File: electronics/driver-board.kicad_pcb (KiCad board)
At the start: 4 copper layers, 40 x 40 mm, 55 parts, among them J1 Conn_01x01_Socket, J10 USB_C_Receptacle_USB2.0, J3 Conn_01x06, J4 Qwiic_RA, J5 Conn_02x03_Counter_Clockwise, J9 Conn_01x01_Socket, SW1 SW_Push, SW2 SW_Push, SW3 SW_Push, SW4 SW_Push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

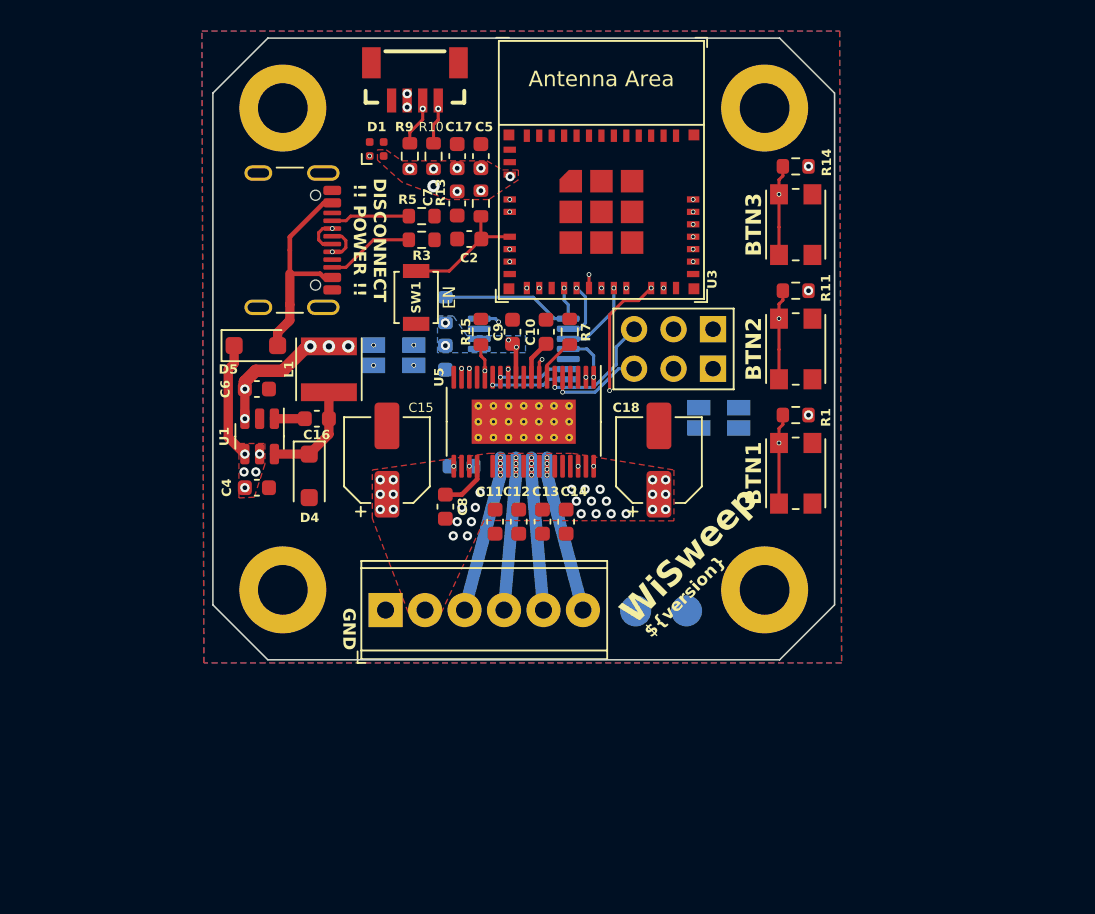
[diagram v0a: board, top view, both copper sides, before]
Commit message: added ldo for USB
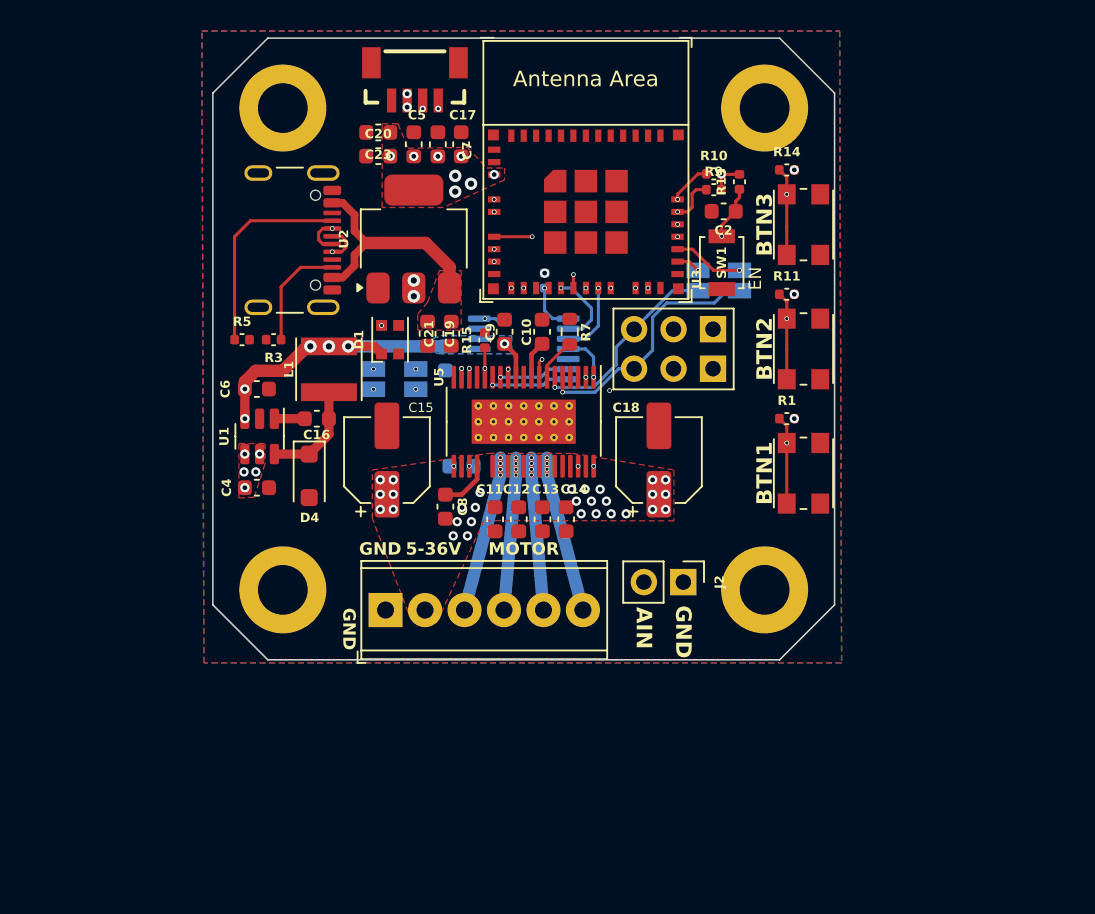
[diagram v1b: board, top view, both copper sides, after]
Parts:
- removed D5: DS210W, Diode_SMD:D_SOD-123F
- removed J1, J9: Conn_01x01_Socket, TestPoint:TestPoint_Pad_D2.0mm
- added C19: 100nF, Capacitor_SMD:C_0603_1608Metric, F.Cu at (43.8, 49.0)
- added C20: 10µF, Capacitor_SMD:C_0603_1608Metric, F.Cu at (40.6, 37.6)
- added C21: 10µF, Capacitor_SMD:C_0603_1608Metric, F.Cu at (45.3, 49.0)
- added C23: 100nF, Capacitor_SMD:C_0603_1608Metric, F.Cu at (40.6, 36.1)
- added J2: Conn_01x02, Connector_PinHeader_2.54mm:PinHeader_1x02_P2.54mm_Vertical, F.Cu at (60.3, 65.0)
- added U2: AMS1117-3.3, Package_TO_SOT_SMD:SOT-223-3_TabPin2, F.Cu at (42.9, 42.9)
- D1: footprint LED_SMD:LED_SK6812_EC15_1.5x1.5mm -> LED_SMD:LED_WS2812B-2020_PLCC4_2.0x2.0mm
- R1, R10, R11, R13, R14, R15, R2, R3, R5, R9: footprint Resistor_SMD:R_0603_1608Metric -> Capacitor_SMD:C_0402_1005Metric
- moved SW1 19.8 mm to (62.7, 44.5)
- moved R9 19.7 mm to (62.2, 39.8), turned to 0 degrees
- moved R10 18.1 mm to (62.2, 38.7), turned to 0 degrees
- moved R13 16.7 mm to (63.9, 39.2)
- moved C2 16.5 mm to (62.9, 41.1)
- moved R5 14.0 mm to (31.9, 49.4)
- moved D1 12.3 mm to (41.4, 49.4)
- moved R3 11.5 mm to (33.9, 49.4), turned to 180 degrees
- moved JP3 8.84 mm to (63.9, 45.6)
- moved JP4 8.84 mm to (61.2, 45.6)
- moved R2 6.66 mm to (51.3, 45.6), turned to 90 degrees
- moved C5 4.38 mm to (42.9, 36.8)
- moved C7 4.01 mm to (44.5, 36.8), turned to -90 degrees
- moved JP1 3.12 mm to (43.1, 51.9)
- moved JP2 3.01 mm to (40.3, 51.9)
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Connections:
- net /USB_VBUS renamed +5V
- net VBUS renamed VM
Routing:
- net /ESP_GPIO3: track 0.00 -> 23.5 mm
- net /TMC_AIN: track 1.22 -> 22.4 mm
- net +3V3: track 12.1 -> 27.9 mm, vias 22 -> 23
- net /ESP_GPIO1: track 0.00 -> 15.4 mm
- net /ESP_EN: track 8.41 -> 18.6 mm, vias 0 -> 2
- net /TMC_REFL: track 6.24 -> 16.3 mm
- net /ESP_GPIO2: track 11.0 -> 20.2 mm
- net /USB_CC1: track 5.06 -> 13.3 mm
- net VM: track 7.45 -> 0.00 mm
- net /ESP_GPIO6: track 10.6 -> 3.19 mm
- net /TMC_REFR: track 8.02 -> 13.2 mm
- net /ESP_GPIO21: track 0.00 -> 4.55 mm
- net /AS_ENCA: track 13.2 -> 10.1 mm
- net /AS_ENCB: track 10.5 -> 13.1 mm
- net /ESP_GPIO7: track 15.7 -> 17.3 mm
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- added copper zone on F.Cu, net +5V
- added copper zone on In1.Cu, net GND
- added copper zone on In2.Cu, net GND
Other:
- board text added: "MOTOR"
- board text removed: "${version}"
- board text removed: "DISCONNECT !! POWER !!"

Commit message: added few ground vias
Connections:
- J4 pad 3: /ESP_GPIO17 -> GND
- J4 pad 4: /ESP_GPIO16 -> GND
- R10 pad 1: /ESP_GPIO16 -> GND
- R9 pad 1: /ESP_GPIO17 -> GND
- U3 pad 30: /ESP_GPIO17 -> GND
- U3 pad 31: /ESP_GPIO16 -> GND
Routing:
- net GND: track 0.07 -> 45.7 mm, vias 0 -> 83
- net /ESP_GPIO17: track 23.7 -> 0.00 mm, vias 2 -> 0
- net /ESP_GPIO16: track 21.9 -> 0.00 mm, vias 2 -> 0
- net /AS_ENCN: track 5.65 -> 4.31 mm
- net VM: vias 34 -> 33

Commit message: reworked layout a bit
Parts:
- removed J2: Conn_01x02, Connector_PinHeader_2.54mm:PinHeader_1x02_P2.54mm_Vertical
- added C1: 100nF, Capacitor_SMD:C_0402_1005Metric, F.Cu at (41.4, 51.8)
- added C24: 100nF, Capacitor_SMD:C_0603_1608Metric, F.Cu at (76.7, 59.2)
- added D2: LESD5D5, Diode_SMD:D_SOD-523, B.Cu at (37.8, 42.2)
- added D6: LESD5D5, Diode_SMD:D_SOD-523, B.Cu at (37.8, 43.8)
- added R6: 10k, Resistor_SMD:R_0402_1005Metric, F.Cu at (76.2, 61.4)
- C22: moved to F.Cu
- R1, R10, R11, R13, R14, R2, R3, R5, R9: footprint Capacitor_SMD:C_0402_1005Metric -> Resistor_SMD:R_0402_1005Metric
- R15: footprint Capacitor_SMD:C_0402_1005Metric -> Resistor_SMD:R_0402_1005Metric; moved to B.Cu
- R7: footprint Resistor_SMD:R_0603_1608Metric -> Resistor_SMD:R_0402_1005Metric
- moved R15 3.56 mm to (48.7, 46.1), turned to 180 degrees
- moved C8 3.02 mm to (44.2, 57.2)
- moved C22 2.21 mm to (44.9, 59.5)
- moved R3 1.39 mm to (32.5, 49.6), turned to -90 degrees
- moved C9 1.12 mm to (48.4, 47.8), turned to 0 degrees
- moved R2 1.05 mm to (52.4, 45.6)
- moved R7 0.93 mm to (52.7, 48.0)
- moved D4 0.86 mm to (35.5, 58.7)
- moved L1 0.86 mm to (36.8, 51.8)
- moved C6 0.86 mm to (32.1, 53.1)
- moved U1 0.86 mm to (32.3, 56.1)
- moved C16 0.86 mm to (36.0, 55.0)
- moved JP2 0.81 mm to (39.5, 51.9)
- moved C15 0.70 mm to (40.5, 57.1)
- moved C18 0.70 mm to (59.4, 57.1)
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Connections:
- J4 pad 3: GND -> /ESP_GPIO17
- J4 pad 4: GND -> /ESP_GPIO16
- R10 pad 1: GND -> /ESP_GPIO16
- R2 pad 1: /ESP_GPIO6 -> /ESP_GPIO7
- R9 pad 1: GND -> /ESP_GPIO17
- U3 pad 30: GND -> /ESP_GPIO17
- U3 pad 31: GND -> /ESP_GPIO16
- U5 pad 1: /ESP_GPIO15 -> /ESP_GPIO14
- U5 pad 2: /ESP_GPIO14 -> /ESP_GPIO6
- U5 pad 36: /ESP_GPIO8 -> /ESP_GPIO15
- U5 pad 38: /ESP_GPIO7 -> /ESP_GPIO8
- U7 pad 1: /ESP_GPIO6 -> /ESP_GPIO7
- U7 pad 2: /ESP_GPIO7 -> /ESP_GPIO8
- U7 pad 3: /ESP_GPIO14 -> /ESP_GPIO6
- U7 pad 4: /ESP_GPIO15 -> /ESP_GPIO14
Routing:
- net GND: track 45.7 -> 0.00 mm, vias 83 -> 106
- net /ESP_GPIO17: track 0.00 -> 24.4 mm, vias 0 -> 2
- net /ESP_GPIO16: track 0.00 -> 22.9 mm, vias 0 -> 2
- net /ESP_GPIO7: track 17.3 -> 2.16 mm, vias 2 -> 1
- net /ESP_GPIO6: track 3.19 -> 11.3 mm, vias 1 -> 2
- net /ESP_GPIO8: track 13.0 -> 18.1 mm, vias 3 -> 2
- net /AS_ENCB: track 13.1 -> 18.1 mm
- net /ESP_GPIO1: track 15.4 -> 10.7 mm
- net /ESP_GPIO15: track 9.35 -> 13.2 mm
- net Net-(U5-CPI): track 0.00 -> 2.53 mm, vias 1 -> 0
- net /ESP_GPIO0: track 8.78 -> 6.26 mm, vias 2 -> 1
- net /BTN1: track 22.6 -> 20.3 mm
- net /AS_ENCA: track 10.1 -> 12.4 mm
- net Net-(U5-CPO): track 0.00 -> 2.26 mm, vias 1 -> 0
- net +3V3: track 27.9 -> 30.2 mm, vias 23 -> 27
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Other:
- board text added: "VM"
- board text removed: "MOTOR"

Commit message: wip usb jtag and power connectors
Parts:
- removed J3: Conn_01x06, TerminalBlock_Phoenix:TerminalBlock_Phoenix_MPT-0,5-6-2.54_1x06_P2.54mm_Horizontal
- removed R11, R14: 10k, Resistor_SMD:R_0402_1005Metric
- removed SW3, SW4: SW_Push, Slimc_Button_Switch_SMD:SW_Push_1P1T_TS-1145-X-B
- added J1: Conn_01x02, Connector_PinHeader_2.00mm:PinHeader_1x02_P2.00mm_Vertical_SMD_Pin1Left, B.Cu at (65.8, 48.6)
- added J2: Conn_01x03, Connector_JST:JST_SH_SM03B-SRSS-TB_1x03-1MP_P1.00mm_Horizontal, B.Cu at (54.0, 67.6)
- added J6: Conn_01x04, Connector_JST:JST_PH_S4B-PH-K_1x04_P2.00mm_Horizontal, F.Cu at (53.0, 63.5)
- added J7: Conn_01x03, Connector_JST:JST_SH_SM03B-SRSS-TB_1x03-1MP_P1.00mm_Horizontal, B.Cu at (46.0, 67.6)
- added R12: 10k, Resistor_SMD:R_0402_1005Metric, F.Cu at (58.8, 46.4)
- added R8: 10k, Resistor_SMD:R_0402_1005Metric, F.Cu at (58.8, 45.3)
- C24, R6: moved to B.Cu
- D2, D6: moved to F.Cu
- J10: footprint Connector_USB:USB_C_Receptacle_GCT_USB4105-xx-A_16P_TopMnt_Horizontal -> Slimc_Connector_USB:USB_C_GT-USB-7036A
- J4: footprint SparkFun-Connector:JST04_1MM_Vertical -> SparkFun-Connector:JST_SMD_1.0mm-4_RA
- J5: value Conn_02x03_Counter_Clockwise -> Conn_01x02; footprint Connector_PinHeader_2.54mm:PinHeader_2x03_P2.54mm_Vertical -> Connector_JST:JST_PH_S2B-PH-K_1x02_P2.00mm_Horizontal
- SW2: footprint Slimc_Button_Switch_SMD:SW_Push_1P1T_TS-1145-X-B -> Button_Switch_SMD:SW_SPST_B3U-1000P
- moved C4 49.5 mm to (82.2, 57.0), turned to -90 degrees
- moved U1 46.6 mm to (78.9, 57.5), turned to 0 degrees
- moved D4 46.1 mm to (81.4, 54.3), turned to 0 degrees
- moved C6 43.9 mm to (75.8, 57.6), turned to -90 degrees
- moved C16 41.8 mm to (77.7, 53.8), turned to -90 degrees
- moved L1 37.8 mm to (74.5, 53.0), turned to 180 degrees
- moved SW2 27.2 mm to (56.3, 33.5)
- moved C17 25.0 mm to (21.1, 39.7)
- moved C7 25.0 mm to (19.7, 39.7)
- moved J4 23.1 mm to (65.2, 38.8)
- moved C5 22.7 mm to (21.1, 42.7), turned to 90 degrees
- moved C1 22.5 mm to (63.9, 52.0)
- moved R1 21.6 mm to (61.3, 33.7), turned to -90 degrees
- moved J5 21.5 mm to (46.9, 63.5), turned to 0 degrees
- moved J10 20.7 mm to (40.9, 62.5), turned to 0 degrees
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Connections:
- net /BTN1 renamed /ESP_BOOT
- J5 pad 2: GND -> VM
- U3 pad 28: /BTN2 -> /ESP_GPIO22
- U3 pad 29: /BTN3 -> /ESP_GPIO23
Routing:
- net /ESP_GPIO17: track 24.4 -> 0.00 mm, vias 2 -> 0
- net +3V3: track 30.2 -> 6.68 mm, vias 27 -> 10
- net /ESP_GPIO3: track 23.0 -> 0.00 mm, vias 2 -> 0
- net /ESP_GPIO16: track 22.9 -> 0.00 mm, vias 2 -> 0
- net /TMC_AIN: track 21.4 -> 0.00 mm, vias 2 -> 0
- net /ESP_GPIO12: track 20.5 -> 0.00 mm, vias 2 -> 0
- net /ESP_GPIO2: track 20.5 -> 0.00 mm, vias 2 -> 0
- net /ESP_BOOT: track 20.3 -> 0.00 mm, vias 2 -> 0
- net /ESP_GPIO13: track 18.9 -> 0.00 mm, vias 2 -> 0
- net /ESP_EN: track 18.5 -> 0.00 mm, vias 2 -> 1
- net /ESP_GPIO8: track 18.1 -> 0.00 mm, vias 2 -> 0
- net /AS_ENCB: track 18.1 -> 0.00 mm, vias 2 -> 0
- net /TMC_REFL: track 17.7 -> 0.00 mm
- net /BTN2: track 15.5 -> 0.00 mm, vias 2 -> 0
- net +5V: track 14.9 -> 0.00 mm
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- removed copper zone on F.Cu, net +3V3
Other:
- board size 40 x 40 mm -> 38.5 x 39.6 mm
- board text added: "IO22"
- board text added: "IO23"
- board text added: "IO9"
- board text added: "NTC"
- board text added: "S"
- board text removed: "AIN"
- board text removed: "BTN1"
- board text removed: "BTN2"
- board text removed: "BTN3"

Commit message: testing new layout
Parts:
- removed C19, C23: 100nF, Capacitor_SMD:C_0603_1608Metric
- removed C20, C21: 10µF, Capacitor_SMD:C_0603_1608Metric
- removed U2: AMS1117-3.3, Package_TO_SOT_SMD:SOT-223-3_TabPin2
- J2, J7: moved to F.Cu
- moved C4 48.3 mm to (34.0, 60.5), turned to 180 degrees
- moved U1 45.3 mm to (33.6, 57.2), turned to -90 degrees
- moved D4 45.0 mm to (36.7, 59.7), turned to -90 degrees
- moved C6 42.6 mm to (33.4, 54.1), turned to 180 degrees
- moved C16 40.6 mm to (37.2, 56.0), turned to 180 degrees
- moved L1 36.5 mm to (38.0, 52.9), turned to 90 degrees
- moved R13 35.8 mm to (39.0, 34.4), turned to 180 degrees
- moved R10 33.6 mm to (41.9, 47.2), turned to -90 degrees
- moved R9 32.6 mm to (41.9, 45.3), turned to 90 degrees
- moved C2 32.4 mm to (41.4, 34.7), turned to 0 degrees
- moved J7 30.8 mm to (61.5, 41.0), turned to 90 degrees
- moved J4 25.1 mm to (40.4, 42.7), turned to -90 degrees
- moved C7 21.9 mm to (41.4, 37.6), turned to 0 degrees
- moved J2 21.5 mm to (61.5, 47.5), turned to 90 degrees
- moved C5 20.6 mm to (41.4, 39.1), turned to 0 degrees
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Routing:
- net GND: track 0.00 -> 17.3 mm
- net /TMC_OUT1B: track 20.7 -> 12.0 mm
- net /TMC_OUT1A: track 20.7 -> 12.0 mm
- net /TMC_OUT2B: track 19.9 -> 11.6 mm
- net VM: track 0.00 -> 8.26 mm
- net /ESP_GPIO12: track 0.00 -> 1.15 mm
- net /TMC_OUT2A: track 19.9 -> 18.7 mm
- net +3V3: vias 10 -> 7
- net /ESP_GPIO5: vias 1 -> 0
- net /ESP_GPIO21: vias 1 -> 0
- net /ESP_GPIO1: vias 1 -> 0
- net /ESP_EN: vias 1 -> 0
- net /AS_ENCN: vias 2 -> 0
- net /AS_ENCA: vias 1 -> 0
- removed copper zone on F.Cu, net +5V
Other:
- board size 38.5 x 39.6 mm -> 38.5 x 39.2 mm
